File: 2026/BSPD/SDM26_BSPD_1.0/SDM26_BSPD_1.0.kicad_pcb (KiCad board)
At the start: 2 copper layers, 46 parts, among them IC1 LM2901BIRTER, IC2 LM2901BIRTER, IC3 SN74HC08PWR, IC4 SN74HC32PWR, IC5 L7805ACD2T-TR, J1 776280-1, Q1 2N7002,215, U1 TPS2116DRL

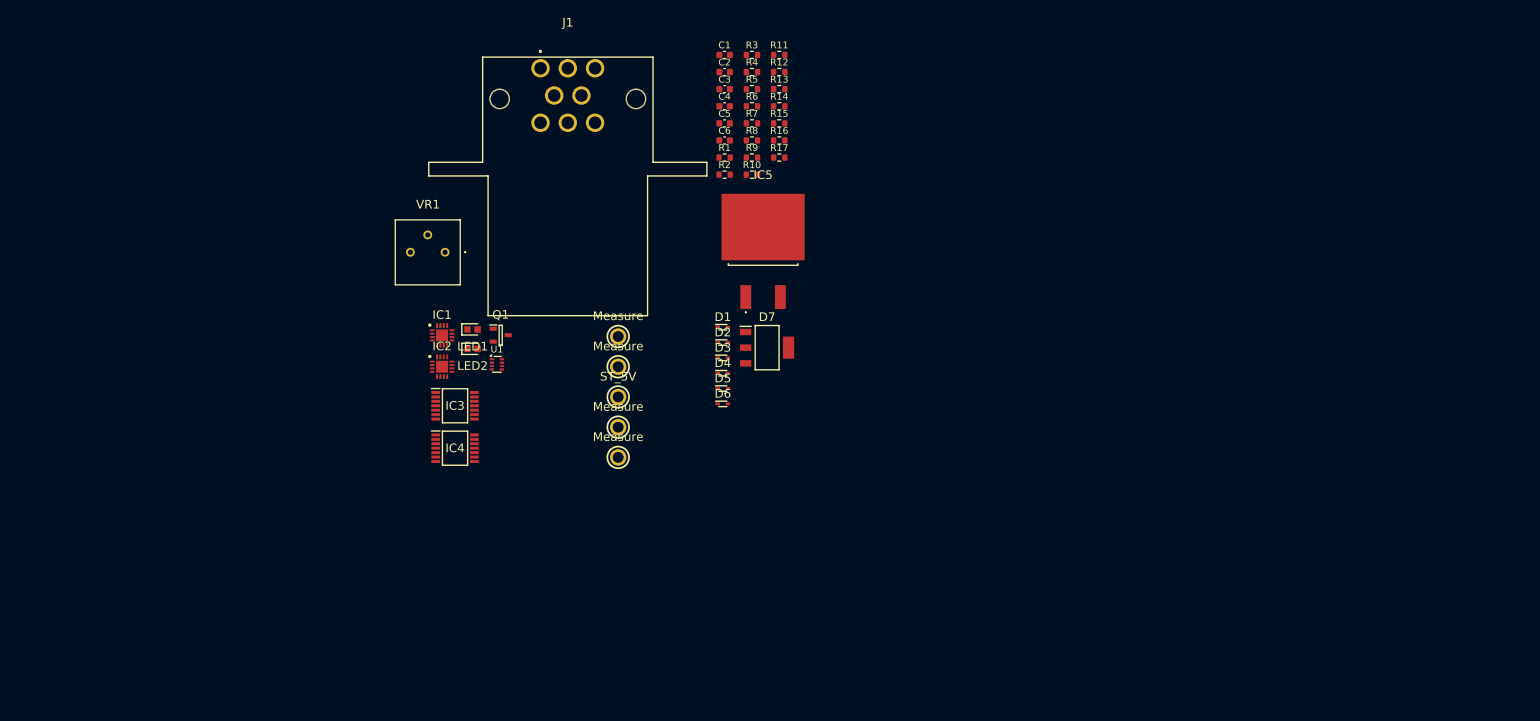
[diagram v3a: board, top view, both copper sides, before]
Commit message: PSBD PCB Logic nearly done
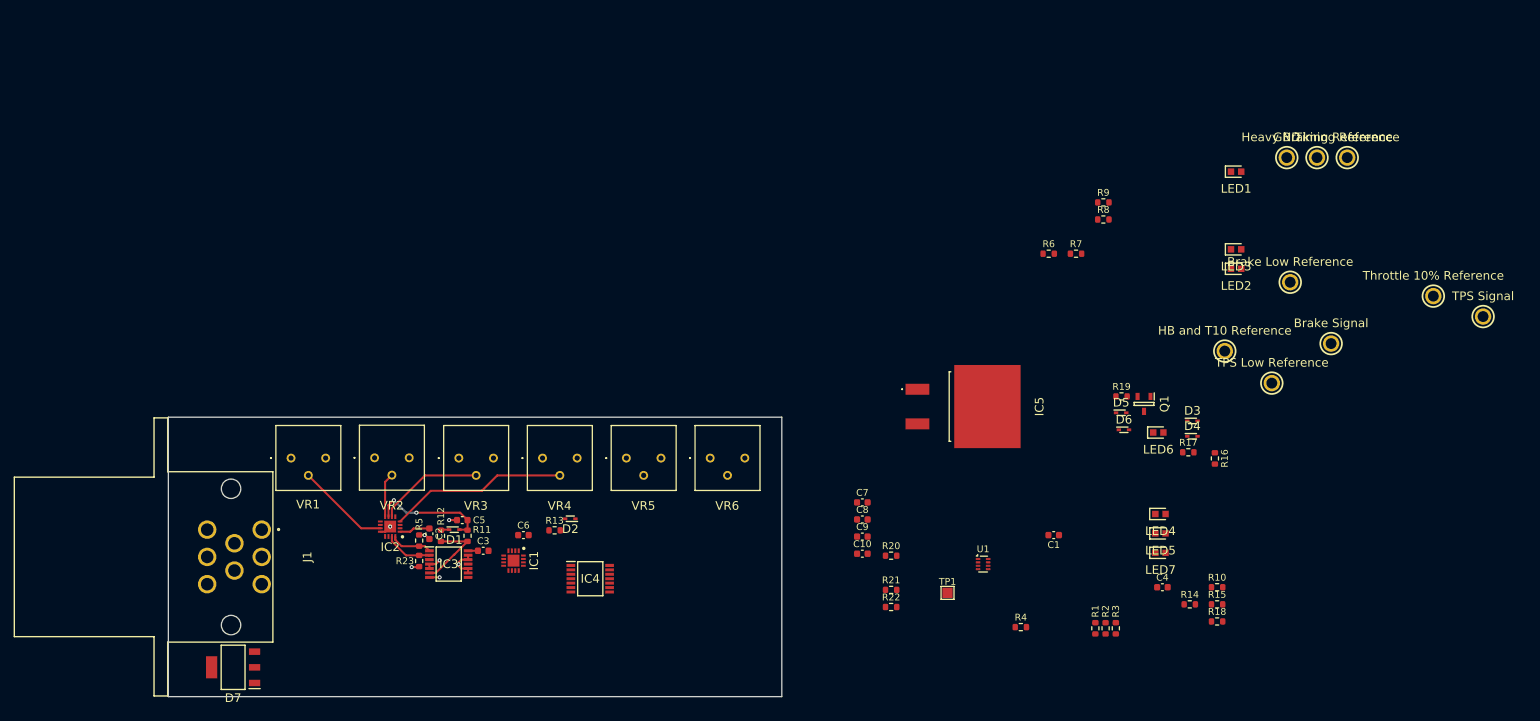
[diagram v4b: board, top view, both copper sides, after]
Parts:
- removed ORANGE_TP1: 5008, SDM_MiscFootprint:5008
- removed YELLOW_TP1: 5009, SDM_MiscFootprint:5009
- added C10: 1uF, Capacitor_SMD:C_0603_1608Metric, F.Cu at (151.8, 120.0)
- added C7: 0.33uF, Capacitor_SMD:C_0603_1608Metric, F.Cu at (151.8, 112.5)
- added C8: 0.1uF, Capacitor_SMD:C_0603_1608Metric, F.Cu at (151.8, 115.0)
- added C9: 1uF, Capacitor_SMD:C_0603_1608Metric, F.Cu at (151.8, 117.5)
- added LED3: 150060RS75000, SDM_MiscFootprint:LEDC1608X80N, F.Cu at (206.7, 75.4)
- added LED4: 150060GS75000, SDM_MiscFootprint:LEDC1608X80N, F.Cu at (195.6, 114.2)
- added LED5: 150060GS75000, SDM_MiscFootprint:LEDC1608X80N, F.Cu at (195.6, 117.0)
- added LED6: 150060GS75000, SDM_MiscFootprint:LEDC1608X80N, F.Cu at (195.2, 102.2)
- added LED7: 150060GS75000, SDM_MiscFootprint:LEDC1608X80N, F.Cu at (195.6, 119.9)
- added R18: 91, Resistor_SMD:R_0603_1608Metric, F.Cu at (203.9, 130.0)
- added R19: 1k, Resistor_SMD:R_0603_1608Metric, F.Cu at (189.8, 97.0)
- added R20: 10k, Resistor_SMD:R_0603_1608Metric, F.Cu at (156.0, 120.3)
- added R21: 10k, Resistor_SMD:R_0603_1608Metric, F.Cu at (156.0, 125.3)
- added R22: 10k, Resistor_SMD:R_0603_1608Metric, F.Cu at (156.0, 127.8)
- added R23: 10k, Resistor_SMD:R_0603_1608Metric, F.Cu at (86.8, 121.1)
- added RED_TP2: 5005, SDM_MiscFootprint:5005, F.Cu at (211.9, 95.0)
- added RED_TP3: 5005, SDM_MiscFootprint:5005, F.Cu at (235.6, 82.2)
- added RED_TP4: 5005, SDM_MiscFootprint:5005, F.Cu at (218.5, 61.9)
- added RED_TP5: 5005, SDM_MiscFootprint:5005, F.Cu at (205.0, 90.3)
- added RED_TP6: 5005, SDM_MiscFootprint:5005, F.Cu at (223.0, 61.9)
- added TP1: ST_5V, TestPoint:TestPoint_Pad_1.5x1.5mm, F.Cu at (164.3, 125.8)
- added VR2: 10k, SDM_MiscFootprint:3386P1103TLF, F.Cu at (80.3, 106.0)
- added VR3: 10k, SDM_MiscFootprint:3386P1103TLF, F.Cu at (92.6, 106.0)
- added VR4: 10k, SDM_MiscFootprint:3386P1103TLF, F.Cu at (104.9, 106.0)
- added VR5: 10k, SDM_MiscFootprint:3386P1103TLF, F.Cu at (117.2, 106.0)
- added VR6: 10k, SDM_MiscFootprint:3386P1103TLF, F.Cu at (129.5, 106.0)
- added WHITE_TP2: 5007, SDM_MiscFootprint:5007, F.Cu at (220.6, 89.2)
- C1, C2: value 10uF -> 0.1uF
- C3: value 0.33uF -> 0.1uF
- C5, C6: value 1uF -> 10uF
- R10: value 100 -> 91
- R11: value 10k -> 100k
- R12: value 470 -> 100
- R13: value 1k -> 10k
- R14: value 10k -> 100
- R15: value 220 -> 91
- R17: value 10k -> 91
- R7: value 100k -> 150
- R8: value 100 -> 510
- R9: value 10k -> 510
- VR1: value 3386P-1-103TLF -> 10k
- moved WHITE_TP1 127.9 mm to (242.9, 85.2)
- moved LED1 114.4 mm to (206.7, 64.0)
- moved LED2 112.6 mm to (206.7, 78.2)
- moved BLACK_TP1 101.5 mm to (214.1, 61.9)
- moved RED_TP1 100.0 mm to (214.6, 80.2)
- moved R3 99.6 mm to (189.0, 131.0), turned to -90 degrees
- moved R15 95.4 mm to (203.9, 127.5)
- moved C4 95.4 mm to (195.9, 125.0)
- moved Q1 94.9 mm to (193.2, 98.0), turned to -90 degrees
- moved R14 94.7 mm to (199.9, 127.5)
- moved D7 91.3 mm to (59.5, 136.7), turned to 180 degrees
- moved R10 91.2 mm to (203.9, 125.0)
- moved R4 90.5 mm to (175.1, 130.8)
- moved R1 87.9 mm to (186.0, 131.0), turned to -90 degrees
- moved R2 86.9 mm to (187.5, 131.0), turned to -90 degrees
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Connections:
- BLACK_TP1 pad 1: unconnected-(BLACK_TP1-Pad1) -> GND
- C1 pad 1: /HB*T10_FAULT -> Net-(IC1-VCC)
- C1 pad 2: GND -> +5V
- C2 pad 1: /BL+TL+(HB*T10)_FAULT -> Net-(IC2-VCC)
- C2 pad 2: GND -> +5V
- C3 pad 1: GND -> Net-(IC3-VCC)
- C3 pad 2: /12V IGNITION -> +5V
- C4 pad 1: GND -> Net-(IC4-VCC)
- C4 pad 2: /5V IGNITION -> +5V
- C5 pad 1: /5V IGNITION -> /HB*T10_FAULT
- C6 pad 1: /5V PDM -> /BL+TL+(HB*T10)_FAULT
- IC1 pad 1: +5V -> Net-(IC1-VCC)
- IC1 pad 11: /TPS_MAIN -> unconnected-(IC1-IN4+-Pad11)
- IC1 pad 13: /TPS_LOW_FAULT -> unconnected-(IC1-OUT4-Pad13)
- IC1 pad 14: /TPS_10%_FAULT -> /TPS_LOW_FAULT
- IC1 pad 15: /HEAVY_BREAKING_FAULT -> unconnected-(IC1-OUT2-Pad15)
- IC1 pad 2: /BRAKE_LOW_REF -> /TPS_LOW_REF
- IC1 pad 4: /BSE -> /TPS_MAIN
- IC1 pad 5: /BSE -> unconnected-(IC1-IN2--Pad5)
- IC1 pad 6: /HEAVY_BREAKING_REF -> unconnected-(IC1-IN2+-Pad6)
- IC1 pad 7: /TPS_MAIN -> /BRAKE_LOW_REF
- IC1 pad 8: /TPS_10%_REF -> /BSE
- IC1 pad 9: /TPS_LOW_REF -> unconnected-(IC1-IN4--Pad9)
- IC2 pad 1: +5V -> Net-(IC2-VCC)
- IC2 pad 11: unconnected-(IC2-IN4+-Pad11) -> /TIMING_REF
- IC2 pad 13: unconnected-(IC2-OUT4-Pad13) -> /BSPD_LOGIC_SIGNAL
- IC2 pad 14: unconnected-(IC2-OUT3-Pad14) -> /HB*T10_1S_FAULT
- IC2 pad 15: /BSPD_LOGIC_SIGNAL -> /TPS_10%_FAULT
- IC2 pad 16: /HB*T10_1S_FAULT -> /HEAVY_BRAKING_FAULT
- IC2 pad 2: /HB*T10_FAULT -> /BSE
- IC2 pad 4: /HB*T10_REF -> /HEAVY_BRAKING_REF
- IC2 pad 5: /BL+TL+(HB*T10)_FAULT -> /TPS_MAIN
- IC2 pad 6: /RC_REF -> /TPS_10%_REF
- IC2 pad 7: unconnected-(IC2-IN3--Pad7) -> /HB*T10_FAULT
- IC2 pad 8: unconnected-(IC2-IN3+-Pad8) -> /HB*T10_REF
- IC2 pad 9: unconnected-(IC2-IN4--Pad9) -> /BL+TL+(HB*T10)_FAULT
- IC3 pad 1: unconnected-(IC3-1A-Pad1) -> /HEAVY_BRAKING_FAULT
- IC3 pad 10: unconnected-(IC3-3B-Pad10) -> GND
- IC3 pad 12: unconnected-(IC3-4A-Pad12) -> GND
- IC3 pad 13: unconnected-(IC3-4B-Pad13) -> GND
- IC3 pad 14: +5V -> Net-(IC3-VCC)
- IC3 pad 2: unconnected-(IC3-1B-Pad2) -> /TPS_10%_FAULT
- IC3 pad 4: /HEAVY_BREAKING_FAULT -> GND
- IC3 pad 5: /TPS_10%_FAULT -> GND
- IC3 pad 9: unconnected-(IC3-3A-Pad9) -> GND
- IC4 pad 10: unconnected-(IC4-3B-Pad10) -> GND
- IC4 pad 12: unconnected-(IC4-4A-Pad12) -> GND
- IC4 pad 13: unconnected-(IC4-4B-Pad13) -> GND
- IC4 pad 14: +5V -> Net-(IC4-VCC)
- IC4 pad 9: unconnected-(IC4-3A-Pad9) -> GND
- J1 pad 1: /12V MASTER -> /TPS_MAIN
- J1 pad 2: GND -> /5V PDM
- J1 pad 4: /TPS_MAIN -> unconnected-(J1-Pin_4-Pad4)
- J1 pad 5: unconnected-(J1-Pin_5-Pad5) -> /12V MASTER
- J1 pad 6: /5V PDM -> /BSE
- J1 pad 7: /BSE -> GND
- LED1 pad 1: BSPD KILL SIGNAL -> GND
- LED2 pad 2: /5V_LED -> Net-(LED2-A)
- R10 pad 1: Net-(IC4-2Y) -> Net-(LED4-A)
- R10 pad 2: Net-(D2-K) -> /BREAK_LOW_FAULT
- R11 pad 1: /12V IGNITION -> Net-(IC3-2Y)
- R11 pad 2: Net-(D5-A) -> /HB*T10_FAULT
- R12 pad 1: Net-(D3-K) -> Net-(IC3-2Y)
- R12 pad 2: Net-(LED1-A) -> Net-(D1-K)
- R13 pad 1: /SCR Gate -> Net-(IC4-2Y)
- R13 pad 2: Net-(D6-K) -> /BL+TL+(HB*T10)_FAULT
- R14 pad 1: +5V -> Net-(IC4-2Y)
- R14 pad 2: Net-(U1-ST) -> Net-(D2-K)
- R15 pad 1: +5V -> Net-(LED5-A)
- R15 pad 2: /5V_LED -> /TPS_LOW_FAULT
- R16 pad 1: /5V PDM -> /12V IGNITION
- R16 pad 2: Net-(U1-PR1) -> Net-(D5-A)
- R17 pad 1: GND -> Net-(D3-K)
- R17 pad 2: Net-(U1-PR1) -> Net-(LED6-A)
- R2 pad 2: /HEAVY_BREAKING_FAULT -> /HEAVY_BRAKING_FAULT
- R3 pad 2: /TPS_10%_FAULT -> /TPS_LOW_FAULT
- R4 pad 2: /TPS_LOW_FAULT -> /HB*T10_1S_FAULT
- R5 pad 2: /HB*T10_1S_FAULT -> /HEAVY_BRAKING_FAULT
- R7 pad 1: Net-(IC3-2Y) -> Net-(LED1-A)
- R7 pad 2: /HB*T10_FAULT -> /5V PDM
- R8 pad 1: Net-(IC3-2Y) -> Net-(LED2-A)
- R8 pad 2: Net-(D1-K) -> /12V MASTER
- R9 pad 1: Net-(IC4-2Y) -> Net-(LED3-A)
- R9 pad 2: /BL+TL+(HB*T10)_FAULT -> /12V IGNITION
- RED_TP1 pad 1: Net-(U1-ST) -> /TIMING_REF
- VR1 pad 1: unconnected-(VR1-CCW-Pad1) -> +5V
- VR1 pad 2: unconnected-(VR1-WIPER-Pad2) -> /TIMING_REF
- VR1 pad 3: unconnected-(VR1-CW-Pad3) -> GND
- WHITE_TP1 pad 1: unconnected-(WHITE_TP1-Pad1) -> /TPS_MAIN
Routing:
- net /HEAVY_BRAKING_REF: track 0.00 -> 26.2 mm
- net /HB*T10_FAULT: track 0.00 -> 17.5 mm, vias 0 -> 2
- net /TPS_10%_REF: track 0.00 -> 15.6 mm
- net /TIMING_REF: track 0.00 -> 13.8 mm
- net GND: track 0.00 -> 11.7 mm, vias 0 -> 5
- net Net-(IC3-2Y): track 0.00 -> 11.4 mm
- net /TPS_10%_FAULT: track 0.00 -> 7.15 mm
- net /HB*T10_REF: track 0.00 -> 6.51 mm
- net /HEAVY_BRAKING_FAULT: track 0.00 -> 6.16 mm
- net Net-(IC2-VCC): track 0.00 -> 4.64 mm
- net +5V: track 0.00 -> 2.88 mm, vias 0 -> 2
- net Net-(IC3-VCC): track 0.00 -> 1.45 mm
- net Net-(D1-K): track 0.00 -> 1.23 mm
- added copper zone on In2.Cu, net +5V
- added copper zone on In1.Cu, net GND
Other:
- board outline added: 90 x 41 mm
- copper layers 2 -> 4

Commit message: Minor fixes
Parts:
- added R7: 10k, Resistor_SMD:R_0603_1608Metric, F.Cu at (55.2, 110.4)
- added R8: 10k, Resistor_SMD:R_0603_1608Metric, F.Cu at (55.2, 112.9)
- moved R16 101.6 mm to (98.8, 117.4), turned to 90 degrees
- moved C4 100.4 mm to (95.5, 123.2), turned to 90 degrees
- moved IC5 61.5 mm to (115.6, 132.4)
- moved IC4 12.2 mm to (99.9, 121.5), turned to 180 degrees
- moved D2 8.33 mm to (100.8, 116.5), turned to 0 degrees
- moved IC1 8.24 mm to (107.8, 117.0)
- moved R15 3.96 mm to (102.8, 117.4), turned to 90 degrees
- moved C6 2.20 mm to (102.0, 115.1), turned to 180 degrees
- moved C3 0.94 mm to (95.5, 120.2), turned to -90 degrees
- renumbered LED3 to LED2, LED2 to LED3, R9 to R10, R8 to R11, R10 to R12, R11 to R13, R12 to R14, R13 to R15, R14 to R16, R15 to R17, R16 to R18, R17 to R19, R3 to R2, R18 to R20, R19 to R21, R20 to R22, R21 to R23, R22 to R24, R5 to R3, R23 to R4, R4 to R5, R7 to R9, RED_TP4 to RED_TP2, RED_TP2 to RED_TP3, RED_TP3 to RED_TP4
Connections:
- C3 pad 1: Net-(IC3-VCC) -> Net-(IC3-3A)
- C4 pad 1: Net-(IC4-VCC) -> Net-(IC4-3A)
- IC3 pad 10: GND -> Net-(IC3-3A)
- IC3 pad 12: GND -> Net-(IC3-3A)
- IC3 pad 13: GND -> Net-(IC3-3A)
- IC3 pad 14: Net-(IC3-VCC) -> Net-(IC3-3A)
- IC3 pad 9: GND -> Net-(IC3-3A)
- IC4 pad 10: GND -> Net-(IC4-3A)
- IC4 pad 12: GND -> Net-(IC4-3A)
- IC4 pad 13: GND -> Net-(IC4-3A)
- IC4 pad 14: Net-(IC4-VCC) -> Net-(IC4-3A)
- IC4 pad 9: GND -> Net-(IC4-3A)
- RED_TP5 pad 1: Net-(VR5-Wiper) -> /TPS_LOW_REF
- RED_TP6 pad 1: Net-(VR6-Wiper) -> /BRAKE_LOW_REF
- VR5 pad 2: Net-(VR5-Wiper) -> /TPS_LOW_REF
- VR6 pad 2: Net-(VR6-Wiper) -> /BRAKE_LOW_REF
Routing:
- net /BL+TL+(HB*T10)_FAULT: track 0.00 -> 28.2 mm, vias 0 -> 2
- net Net-(IC4-2Y): track 0.00 -> 7.71 mm
- net Net-(IC3-3A): track 0.00 -> 7.14 mm
- net Net-(IC4-3A): track 0.00 -> 6.91 mm
- net GND: track 11.7 -> 9.19 mm, vias 5 -> 6
- net +5V: track 2.88 -> 4.33 mm, vias 2 -> 3
- net Net-(IC3-VCC): track 1.45 -> 0.00 mm
- net Net-(D2-K): track 0.00 -> 1.28 mm
- net /BL+TL_FAULT: track 0.00 -> 0.65 mm

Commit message: Computer Sync
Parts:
- removed the R2 at (189.0, 131.0)
- IC1, IC2: footprint SDM_MiscFootprint:QFN50P300X300X80-17L-D -> SDM_MiscFootprint:QFN50P300X300X80-17N-D
- moved R7 66.2 mm to (121.1, 115.9)
- moved R8 66.2 mm to (121.1, 118.4)
- moved IC5 64.3 mm to (179.9, 132.9)
- moved VR2 51.0 mm to (131.3, 106.0)
- moved C2 51.0 mm to (139.3, 117.1)
- moved D2 51.0 mm to (151.8, 116.5)
- moved IC2 51.0 mm to (133.6, 116.0)
- moved R15 51.0 mm to (153.8, 117.4)
- moved R16 51.0 mm to (149.8, 117.4)
- moved R3 51.0 mm to (137.8, 118.1)
- moved R4 51.0 mm to (137.8, 121.1)
- moved C3 51.0 mm to (146.5, 120.2)
- moved C4 51.0 mm to (146.5, 123.2)
- moved C5 51.0 mm to (144.1, 115.1)
- moved C6 51.0 mm to (153.0, 115.1)
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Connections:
- R2 pad 2: /HEAVY_BRAKING_FAULT -> /TPS_LOW_FAULT
- RED_TP1 pad 1: /TIMING_REF -> unconnected-(RED_TP1-Pad1)
- RED_TP2 pad 1: /HB*T10_REF -> unconnected-(RED_TP2-Pad1)
- RED_TP3 pad 1: /TPS_10%_REF -> unconnected-(RED_TP3-Pad1)
- RED_TP4 pad 1: /HEAVY_BRAKING_REF -> unconnected-(RED_TP4-Pad1)
- RED_TP5 pad 1: /TPS_LOW_REF -> unconnected-(RED_TP5-Pad1)
- RED_TP6 pad 1: /BRAKE_LOW_REF -> unconnected-(RED_TP6-Pad1)
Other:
- board size 90 x 41 mm -> 91 x 40 mm
